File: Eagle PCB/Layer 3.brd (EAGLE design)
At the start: 108.5 x 108.5 mm, 86 parts, among them Q1 AO3402, Q2 AO3402, X1 SM06B-SRSS-TB, Y1 8MHz

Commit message: Final
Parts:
- moved R1 2.89 mm to (-10.9, 17.1)
- moved S1 0.46 mm to (-15.3, 14.4), flipped to the top, turned to 180 degrees
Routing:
- net GND: track 171.1 -> 159.5 mm, vias 22 -> 19
- net DIP1: track 42.3 -> 33.5 mm, vias 2 -> 3
- net DIP4: track 51.6 -> 43.3 mm, vias 0 -> 1
- net TX1_ST2: track 96.9 -> 89.6 mm
- net DIP3: track 49.6 -> 44.4 mm, vias 1 -> 2
- net DIP2: track 45.6 -> 40.5 mm, vias 3 -> 4
- net RX1_ST2: track 96.9 -> 92.2 mm
- net 3V3_SWITCH: track 517.1 -> 520.6 mm
- net N$72: track 37.5 -> 34.5 mm

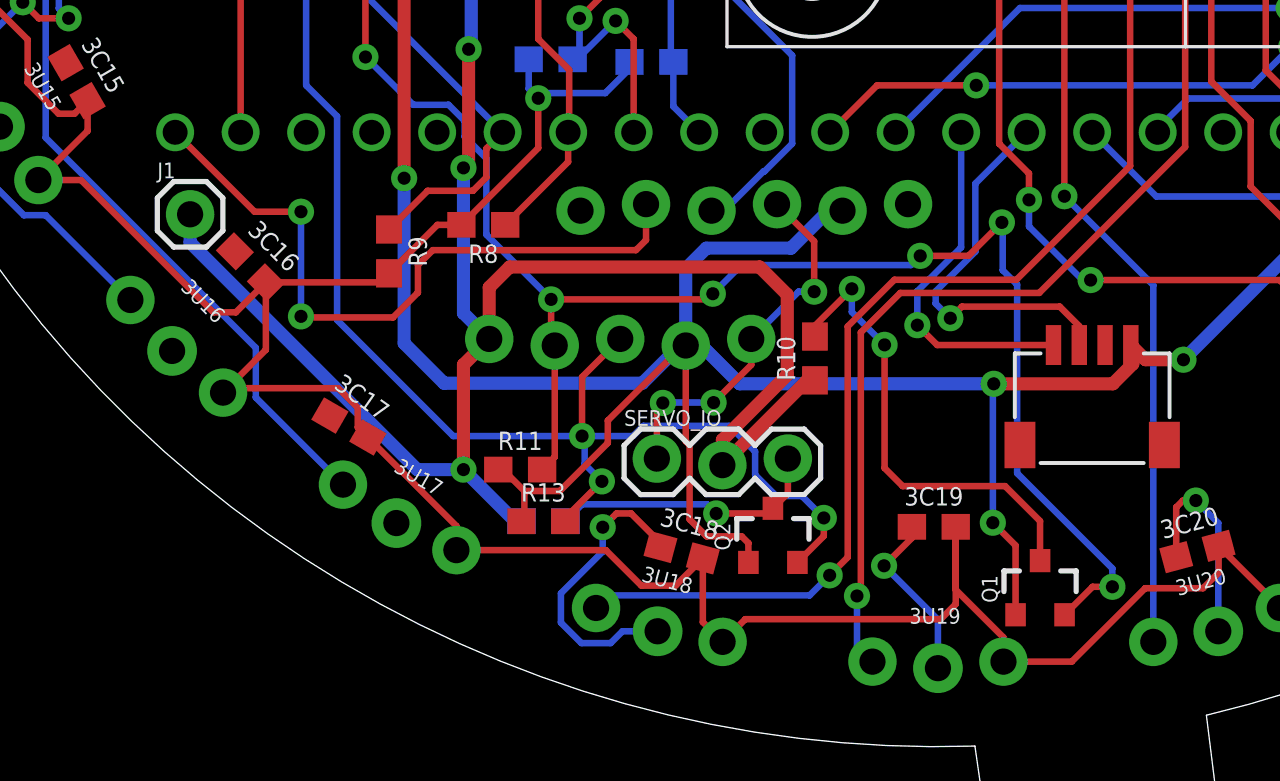
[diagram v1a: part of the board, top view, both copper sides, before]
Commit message: layer 1 esc fix
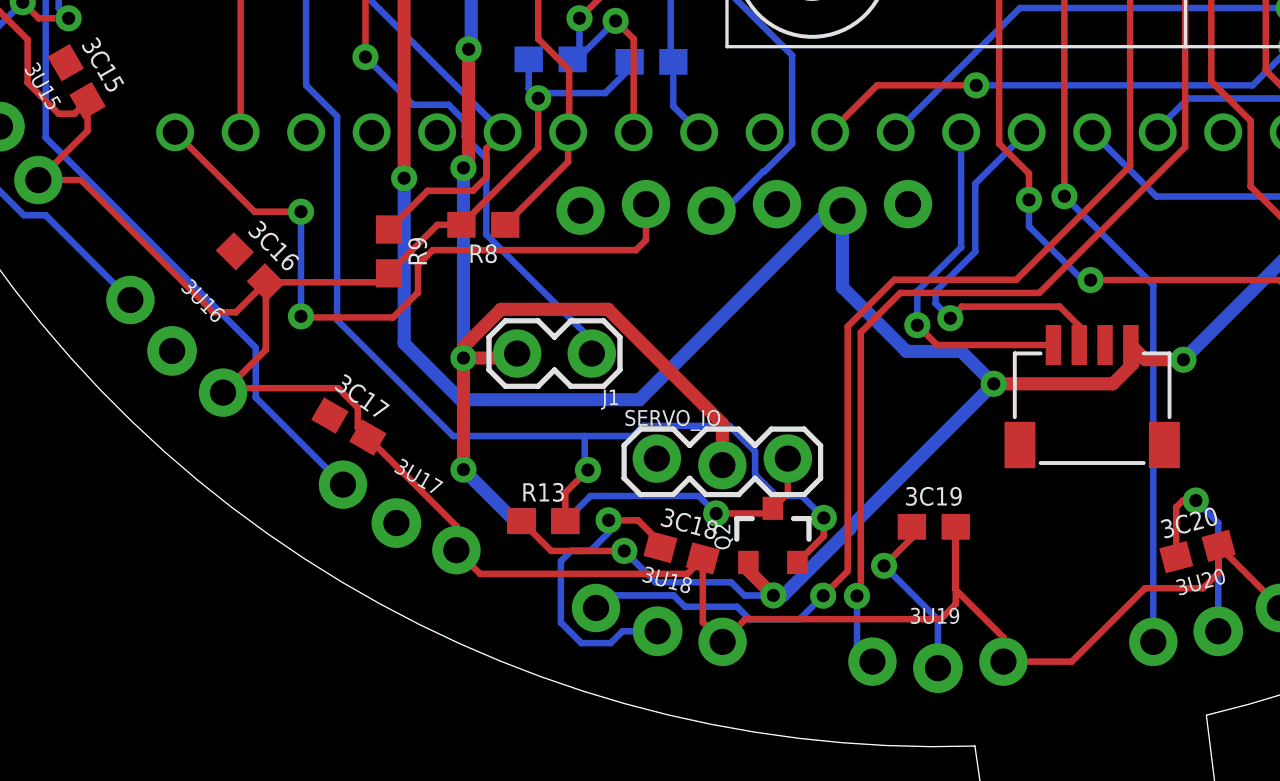
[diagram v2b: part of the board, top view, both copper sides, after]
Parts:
- removed 2ND_LAYER: (no value), SparkFun-Connectors:1X05_LOCK
- removed Q1: AO3402, SparkFun-DiscreteSemi:SOT23-3
- removed R10, R11: 4.7k, JH:R0603
- J1: device Connectors:1X01 -> Connectors:1X02_LOCK
- moved J1 16.3 mm to (-13.6, -29.8), turned to 180 degrees
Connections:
- removed net ESC_HV: Q1.3, R10.2
- net 3.3V: no longer 2ND_LAYER.2, Q1.1, R11.1
- net 5V: now also J1.2; no longer 2ND_LAYER.5, J1.1, R10.1
- net ESC_LV: now also J1.1; no longer 2ND_LAYER.4, Q1.2, R11.2
- net GND: no longer 2ND_LAYER.1
- net SERVO_LV: no longer 2ND_LAYER.3
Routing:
- net ESC_LV: track 69.4 -> 28.4 mm, vias 7 -> 2
- net 5V: track 84.1 -> 57.7 mm, vias 4 -> 5
- net ESC_HV: track 18.3 -> 0.00 mm, vias 2 -> 0
- net GND: track 159.5 -> 145.2 mm, vias 19 -> 16
- net 3.3V: track 150.4 -> 140.4 mm, vias 7 -> 8
- net SERVO_LV: track 56.6 -> 51.8 mm, vias 3 -> 2
- net IR18: track 136.0 -> 137.1 mm
